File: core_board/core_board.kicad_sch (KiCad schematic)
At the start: 16 parts

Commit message: small updates
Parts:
- removed J?: Conn_01x04_Male, symbol Connector:Conn_01x04_Male
- removed J? (x6): Conn_02x25_Top_Bottom, symbol Connector_Generic:Conn_02x25_Top_Bottom
- added J?: Dsub, symbol Connector_Generic:Conn_02x25_Top_Bottom
- added R?: 10k, symbol Device:R_Small_US
- added U?: TCA9535PWR, SOP65P640X120-24N, symbol TCA9535PWR:TCA9535PWR
- J?: value Conn_01x03_Male -> UART Pins
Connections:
- net +3V3: now also R?.1, U?.24 (VCC)
- net GND: now also U?.12 (GND), U?.2 (A1), U?.21 (A0), U?.3 (A2)
- net Extra_Input_A renamed INT_0
- net INT_0: now also R?.2, U?.1 (~{INT})
- net Extra_Input_B renamed INT_1
- net Extra_Input_C renamed INT_2
- net Extra_Input_D renamed INT_3
- net I2C_SCL_A renamed I2C_SCL_0
- net I2C_SCL_B renamed I2C_SCL_1
- net I2C_SCL_C renamed I2C_SCL_2
- net I2C_SCL_Expander_A renamed Broadcast_A
- net I2C_SCL_Expander_B renamed Broadcast_C
- net I2C_SDA_A renamed I2C_SDA_1
- net I2C_SDA_B renamed I2C_SDA_2
- net I2C_SDA_C renamed I2C_SDA_3
- net I2C_SDA_Expander_A renamed INT_5
- net I2C_SDA_Expander_B renamed Broadcast_B
- net IGNITE renamed INT_4
- net SPI_CS_0 renamed I2C_SDA_0
- net SPI_CS_1 renamed I2C_SCL_3
- net SPI_CS_2 renamed I2C_SDA_4
- net SPI_CS_3 renamed I2C_SCL_4
- net SPI_CS_4 renamed I2C_SDA_5
- net SPI_CS_5 renamed I2C_SCL_5
- net SPI_MISO renamed I2C_SDA_IO_Expander
- net I2C_SDA_IO_Expander: now also U?.23 (SDA)
- net SPI_MOSI renamed I2C_SCL_IO_Expander
- net I2C_SCL_IO_Expander: now also U?.22 (SCL)
- net SPI_SCK renamed Broadcast_D
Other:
- note added: "TODO: Add pullip resistors for I2C and I/O"
- note added: "TODO: Add testpoints for logic analyzer"
- note removed: "TODO: Add I/O Expanders"
- note removed: "TODO: Add components for DC-DC converter"
- moved on the sheet: JP?, R?, U?

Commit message: finished schematic
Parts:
- removed D?: D_Schottky, symbol Device:D_Schottky
- removed R?: 10k, symbol Device:R_Small_US
- removed U?: TPS54332DDAR, VREG_LM5017MR/NOPB, symbol TPS54332DDAR:TPS54332DDAR
- added C? (x2): 10uF, symbol Device:C_Small
- added C? (x4): 47uF, symbol Device:C_Small
- added C?: 145pF, symbol Device:C_Small
- added C?: 90pF, symbol Device:C_Small
- added C?: 5pF, symbol Device:C_Small
- added C?: 8pF, symbol Device:C_Small
- added C? (x2): 15nF, symbol Device:C_Small
- added C? (x2): 0.1uF, symbol Device:C_Small
- added D? (x2): B340, Diode_SMD:D_SMC, symbol Diode:B340
- added D?: 40V, Diode_SMD:D_0603_1608Metric, symbol Device:D_Schottky
- added J? (x5): Dsub, symbol Connector_Generic:Conn_02x25_Top_Bottom
- added J?: Testpoints, symbol Connector_Generic:Conn_02x10_Odd_Even
- added L?: 2.85uH, symbol Device:L_Small
- added L?: 3.5uH, symbol Device:L_Small
- added R? (x14): 4.7k, symbol Device:R_Small_US
- added R? (x3): 150k, symbol Device:R_Small_US
- added R? (x8): 10k, symbol Device:R_Small_US
- added R? (x2): 1M, symbol Device:R_Small_US
- added R?: 3.2k, symbol Device:R_Small_US
- added R?: 95k, symbol Device:R_Small_US
- added R? (x2): 50k, symbol Device:R_Small_US
- added R?: 1.9k, symbol Device:R_Small_US
- added U? (x5): TCA9535PWR, SOP65P640X120-24N, symbol TCA9535PWR:TCA9535PWR
- added U?: TPS54332DDAR, VREG_LM5017MR/NOPB, symbol TPS54332DDAR:TPS54332DDAR
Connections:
- net +12V is gone; now on net 12V: J?.2 (Pin_2), U?.2 (VIN)
- net +3V3 is gone; now on net 3V3: U?.24 (VCC)
- net Broadcast_A: now also J?.3 (Pin_3), U?.15 (IO13), J?.15 (Pin_15), J?.3 (Pin_3), J?.3 (Pin_3), J?.3 (Pin_3), J?.3 (Pin_3), J?.3 (Pin_3); no longer U?.9 (IO25)
- net Broadcast_B: now also J?.4 (Pin_4), U?.13 (IO12), J?.16 (Pin_16), J?.4 (Pin_4), J?.4 (Pin_4), J?.4 (Pin_4), J?.4 (Pin_4), J?.4 (Pin_4); no longer U?.10 (IO26)
- net Broadcast_C: now also J?.5 (Pin_5), U?.10 (IO26), J?.17 (Pin_17), J?.5 (Pin_5), J?.5 (Pin_5), J?.5 (Pin_5), J?.5 (Pin_5), J?.5 (Pin_5); no longer U?.11 (IO27)
- net Broadcast_D: now also J?.6 (Pin_6), U?.9 (IO25), J?.18 (Pin_18), J?.6 (Pin_6), J?.6 (Pin_6), J?.6 (Pin_6), J?.6 (Pin_6), J?.6 (Pin_6); no longer U?.12 (IO14)
- net GND: now also J?.1 (Pin_1), J?.23 (Pin_23), J?.24 (Pin_24), J?.25 (Pin_25), J?.26 (Pin_26), J?.27 (Pin_27), J?.28 (Pin_28), J?.29 (Pin_29), C?.1, C?.1, C?.1, C?.1, C?.2, C?.2, C?.2, C?.2, C?.2, C?.2, D?.2 (A), D?.2 (A), D?.2 (A), J?.19 (Pin_19), J?.20 (Pin_20), J?.23 (Pin_23), J?.23 (Pin_23), J?.23 (Pin_23), J?.23 (Pin_23), J?.23 (Pin_23), J?.24 (Pin_24), J?.24 (Pin_24), J?.24 (Pin_24), J?.24 (Pin_24), J?.24 (Pin_24), J?.25 (Pin_25), J?.25 (Pin_25), J?.25 (Pin_25), J?.25 (Pin_25), J?.25 (Pin_25), J?.26 (Pin_26), J?.26 (Pin_26), J?.26 (Pin_26), J?.26 (Pin_26), J?.26 (Pin_26), J?.27 (Pin_27), J?.27 (Pin_27), J?.27 (Pin_27), J?.27 (Pin_27), J?.27 (Pin_27), J?.28 (Pin_28), J?.28 (Pin_28), J?.28 (Pin_28), J?.28 (Pin_28), J?.28 (Pin_28), J?.29 (Pin_29), J?.29 (Pin_29), J?.29 (Pin_29), J?.29 (Pin_29), J?.29 (Pin_29), R?.1, R?.1, R?.1, R?.1, R?.1, R?.1, R?.2, R?.2, U?.12 (GND), U?.12 (GND), U?.12 (GND), U?.12 (GND), U?.12 (GND), U?.2 (A1), U?.2 (A1), U?.2 (A1), U?.2 (A1), U?.21 (A0), U?.21 (A0), U?.21 (A0), U?.3 (A2), U?.3 (A2), U?.3 (A2), U?.7 (GND), U?.9 (EP); no longer U?.2 (A1), U?.21 (A0)
- net I2C_SCL_0: now also U?.21 (IO23), J?.2 (Pin_2), J?.2 (Pin_2), R?.2; no longer U?.22 (IO22)
- net I2C_SCL_1: now also U?.22 (IO22), J?.2 (Pin_2), J?.4 (Pin_4), R?.2; no longer U?.27 (IO19)
- net I2C_SCL_2: now also U?.28 (IO18), J?.2 (Pin_2), J?.6 (Pin_6), R?.2; no longer U?.29 (IO5)
- net I2C_SCL_3: now also J?.2 (Pin_2), U?.30 (IO17), J?.8 (Pin_8), R?.2; no longer U?.31 (IO16)
- net I2C_SCL_4: now also U?.32 (IO4), J?.10 (Pin_10), J?.2 (Pin_2), R?.2; no longer U?.33 (IO0)
- net I2C_SCL_5: now also U?.34 (IO2), J?.12 (Pin_12), J?.2 (Pin_2), R?.2; no longer U?.35 (IO15)
- net I2C_SDA_0: now also U?.25 (IO21), J?.1 (Pin_1), J?.1 (Pin_1), R?.2; no longer U?.21 (IO23)
- net I2C_SDA_1: now also U?.27 (IO19), J?.1 (Pin_1), J?.3 (Pin_3), R?.2; no longer U?.25 (IO21)
- net I2C_SDA_2: now also U?.29 (IO5), J?.1 (Pin_1), J?.5 (Pin_5), R?.2; no longer U?.28 (IO18)
- net I2C_SDA_3: now also J?.1 (Pin_1), U?.31 (IO16), J?.7 (Pin_7), R?.2; no longer U?.30 (IO17)
- net I2C_SDA_4: now also U?.33 (IO0), J?.1 (Pin_1), J?.9 (Pin_9), R?.2; no longer U?.32 (IO4)
- net I2C_SDA_5: now also U?.35 (IO15), J?.1 (Pin_1), J?.11 (Pin_11), R?.2; no longer U?.34 (IO2)
- net INT_0: now also R?.2, U?.1 (~{INT}); no longer U?.1 (~{INT})
- net INT_1: now also R?.2, U?.1 (~{INT})
- net INT_2: now also R?.2, U?.1 (~{INT})
- net INT_3: now also U?.1 (~{INT}), R?.2
- net INT_4: now also R?.2, U?.1 (~{INT})
- net INT_5: now also R?.2, U?.1 (~{INT})
- net IO_3_06: now reaches U?.10 (P06)
- net IO_3_06: now also J?.13 (Pin_13)
- net IO_3_07: now reaches U?.11 (P07)
- net IO_3_07: now also J?.14 (Pin_14)
- net IO_3_08: now reaches U?.13 (P10)
- net IO_3_08: now also J?.15 (Pin_15)
- net IO_3_09: now reaches U?.14 (P11)
- net IO_3_09: now also J?.16 (Pin_16)
- net IO_3_10: now reaches U?.15 (P12)
- net IO_3_10: now also J?.17 (Pin_17)
- net IO_3_11: now reaches U?.16 (P13)
- net IO_3_11: now also J?.18 (Pin_18)
- net IO_3_12: now reaches U?.17 (P14)
- net IO_3_12: now also J?.19 (Pin_19)
- net IO_3_13: now reaches U?.18 (P15)
- net IO_3_13: now also J?.20 (Pin_20)
- net IO_3_14: now reaches U?.19 (P16)
- net IO_3_14: now also J?.21 (Pin_21)
- net IO_3_15: now reaches U?.20 (P17)
- net IO_3_15: now also J?.22 (Pin_22)
- net IO_3_00: now reaches U?.4 (P00)
- net IO_3_00: now also J?.7 (Pin_7)
- net IO_3_01: now reaches U?.5 (P01)
- net IO_3_01: now also J?.8 (Pin_8)
- net IO_3_02: now reaches U?.6 (P02)
- net IO_3_02: now also J?.9 (Pin_9)
- net IO_3_03: now reaches U?.7 (P03)
- net IO_3_03: now also J?.10 (Pin_10)
- net IO_3_04: now reaches U?.8 (P04)
- net IO_3_04: now also J?.11 (Pin_11)
- net IO_3_05: now reaches U?.9 (P05)
- net IO_3_05: now also J?.12 (Pin_12)
- net at U?.1 (BOOT): now also C?.2
- net at U?.3 (EN): now also R?.1, R?.2
- net at U?.4 (SS): now also C?.2, R?.2
- net at U?.5 (VSENSE): now also R?.1, R?.2
- net at U?.6 (COMP): now also C?.2, C?.2
- net at U?.8 (PH): now also C?.1, D?.1 (K), L?.1
- net 3V3: now reaches J?.30 (Pin_30)
- net 3V3: now also J?.31 (Pin_31), J?.32 (Pin_32), J?.33 (Pin_33), J?.34 (Pin_34), J?.35 (Pin_35), J?.36 (Pin_36), U?.2 (A1), U?.21 (A0), C?.1, C?.1, J?.30 (Pin_30), J?.30 (Pin_30), J?.30 (Pin_30), J?.30 (Pin_30), J?.30 (Pin_30), J?.31 (Pin_31), J?.31 (Pin_31), J?.31 (Pin_31), J?.31 (Pin_31), J?.31 (Pin_31), J?.32 (Pin_32), J?.32 (Pin_32), J?.32 (Pin_32), J?.32 (Pin_32), J?.32 (Pin_32), J?.33 (Pin_33), J?.33 (Pin_33), J?.33 (Pin_33), J?.33 (Pin_33), J?.33 (Pin_33), J?.34 (Pin_34), J?.34 (Pin_34), J?.34 (Pin_34), J?.34 (Pin_34), J?.34 (Pin_34), J?.35 (Pin_35), J?.35 (Pin_35), J?.35 (Pin_35), J?.35 (Pin_35), J?.35 (Pin_35), J?.36 (Pin_36), J?.36 (Pin_36), J?.36 (Pin_36), J?.36 (Pin_36), J?.36 (Pin_36), L?.2, R?.1, R?.1, R?.1, R?.1, R?.1, R?.1, R?.1, R?.1, R?.1, R?.1, R?.1, R?.1, R?.1, R?.1, R?.1, R?.1, R?.1, R?.1, R?.1, R?.1, R?.2, U?.2 (A1), U?.21 (A0), U?.21 (A0), U?.24 (VCC), U?.24 (VCC), U?.24 (VCC), U?.24 (VCC), U?.24 (VCC), U?.3 (A2), U?.3 (A2)
- net 5V: now reaches J?.37 (Pin_37)
- net 5V: now also J?.38 (Pin_38), J?.39 (Pin_39), J?.40 (Pin_40), J?.41 (Pin_41), J?.42 (Pin_42), J?.43 (Pin_43), JP?.1 (A), C?.1, C?.1, J?.37 (Pin_37), J?.37 (Pin_37), J?.37 (Pin_37), J?.37 (Pin_37), J?.37 (Pin_37), J?.38 (Pin_38), J?.38 (Pin_38), J?.38 (Pin_38), J?.38 (Pin_38), J?.38 (Pin_38), J?.39 (Pin_39), J?.39 (Pin_39), J?.39 (Pin_39), J?.39 (Pin_39), J?.39 (Pin_39), J?.40 (Pin_40), J?.40 (Pin_40), J?.40 (Pin_40), J?.40 (Pin_40), J?.40 (Pin_40), J?.41 (Pin_41), J?.41 (Pin_41), J?.41 (Pin_41), J?.41 (Pin_41), J?.41 (Pin_41), J?.42 (Pin_42), J?.42 (Pin_42), J?.42 (Pin_42), J?.42 (Pin_42), J?.42 (Pin_42), J?.43 (Pin_43), J?.43 (Pin_43), J?.43 (Pin_43), J?.43 (Pin_43), J?.43 (Pin_43), L?.2, R?.2
- net 12V: now reaches J?.44 (Pin_44)
- net 12V: now also J?.45 (Pin_45), J?.46 (Pin_46), J?.47 (Pin_47), J?.48 (Pin_48), J?.49 (Pin_49), J?.50 (Pin_50), C?.1, C?.1, D?.1 (K), J?.44 (Pin_44), J?.44 (Pin_44), J?.44 (Pin_44), J?.44 (Pin_44), J?.44 (Pin_44), J?.45 (Pin_45), J?.45 (Pin_45), J?.45 (Pin_45), J?.45 (Pin_45), J?.45 (Pin_45), J?.46 (Pin_46), J?.46 (Pin_46), J?.46 (Pin_46), J?.46 (Pin_46), J?.46 (Pin_46), J?.47 (Pin_47), J?.47 (Pin_47), J?.47 (Pin_47), J?.47 (Pin_47), J?.47 (Pin_47), J?.48 (Pin_48), J?.48 (Pin_48), J?.48 (Pin_48), J?.48 (Pin_48), J?.48 (Pin_48), J?.49 (Pin_49), J?.49 (Pin_49), J?.49 (Pin_49), J?.49 (Pin_49), J?.49 (Pin_49), J?.50 (Pin_50), J?.50 (Pin_50), J?.50 (Pin_50), J?.50 (Pin_50), J?.50 (Pin_50), R?.2, R?.2, U?.2 (VIN)
- removed net +5V: J?.1 (Pin_1), JP?.1 (A)
- net I2C_SCL_IO_Expander renamed I2C_SCL_Exp
- net I2C_SCL_Exp: now also U?.11 (IO27), J?.14 (Pin_14), R?.2, U?.22 (SCL), U?.22 (SCL), U?.22 (SCL), U?.22 (SCL), U?.22 (SCL); no longer U?.15 (IO13)
- net I2C_SDA_IO_Expander renamed I2C_SDA_Exp
- net I2C_SDA_Exp: now also U?.12 (IO14), J?.13 (Pin_13), R?.2, U?.23 (SDA), U?.23 (SDA), U?.23 (SDA), U?.23 (SDA), U?.23 (SDA); no longer U?.13 (IO12)
- new net: C?.1, D?.1 (K), L?.1, U?.8 (PH)
- new net: R?.1, R?.2, U?.3 (EN)
- new net: R?.1, R?.2, U?.5 (VSENSE)
- new net: C?.1, R?.1 (x2)
- new net: C?.2, R?.2, U?.4 (SS)
- new net: C?.2, C?.2, U?.6 (COMP)
- new net: C?.2, U?.1 (BOOT)
- new net IO_0_00: J?.7 (Pin_7), U?.4 (P00)
- new net IO_0_01: J?.8 (Pin_8), U?.5 (P01)
- new net IO_0_02: J?.9 (Pin_9), U?.6 (P02)
- new net IO_0_03: J?.10 (Pin_10), U?.7 (P03)
- new net IO_0_04: J?.11 (Pin_11), U?.8 (P04)
- new net IO_0_05: J?.12 (Pin_12), U?.9 (P05)
- new net IO_0_06: J?.13 (Pin_13), U?.10 (P06)
- new net IO_0_07: J?.14 (Pin_14), U?.11 (P07)
- new net IO_0_08: J?.15 (Pin_15), U?.13 (P10)
- new net IO_0_09: J?.16 (Pin_16), U?.14 (P11)
- new net IO_0_10: J?.17 (Pin_17), U?.15 (P12)
- new net IO_0_11: J?.18 (Pin_18), U?.16 (P13)
- new net IO_0_12: J?.19 (Pin_19), U?.17 (P14)
- new net IO_0_13: J?.20 (Pin_20), U?.18 (P15)
- new net IO_0_14: J?.21 (Pin_21), U?.19 (P16)
- new net IO_0_15: J?.22 (Pin_22), U?.20 (P17)
- new net IO_1_00: J?.7 (Pin_7), U?.4 (P00)
- new net IO_1_01: J?.8 (Pin_8), U?.5 (P01)
- new net IO_1_02: J?.9 (Pin_9), U?.6 (P02)
- new net IO_1_03: J?.10 (Pin_10), U?.7 (P03)
- new net IO_1_04: J?.11 (Pin_11), U?.8 (P04)
- new net IO_1_05: J?.12 (Pin_12), U?.9 (P05)
- new net IO_1_06: J?.13 (Pin_13), U?.10 (P06)
- new net IO_1_07: J?.14 (Pin_14), U?.11 (P07)
- new net IO_1_08: J?.15 (Pin_15), U?.13 (P10)
- new net IO_1_09: J?.16 (Pin_16), U?.14 (P11)
- new net IO_1_10: J?.17 (Pin_17), U?.15 (P12)
- new net IO_1_11: J?.18 (Pin_18), U?.16 (P13)
- new net IO_1_12: J?.19 (Pin_19), U?.17 (P14)
- new net IO_1_13: J?.20 (Pin_20), U?.18 (P15)
- new net IO_1_14: J?.21 (Pin_21), U?.19 (P16)
- new net IO_1_15: J?.22 (Pin_22), U?.20 (P17)
- new net IO_2_00: J?.7 (Pin_7), U?.4 (P00)
- new net IO_2_01: J?.8 (Pin_8), U?.5 (P01)
- new net IO_2_02: J?.9 (Pin_9), U?.6 (P02)
- new net IO_2_03: J?.10 (Pin_10), U?.7 (P03)
- new net IO_2_04: J?.11 (Pin_11), U?.8 (P04)
- new net IO_2_05: J?.12 (Pin_12), U?.9 (P05)
- new net IO_2_06: J?.13 (Pin_13), U?.10 (P06)
- new net IO_2_07: J?.14 (Pin_14), U?.11 (P07)
- new net IO_2_08: J?.15 (Pin_15), U?.13 (P10)
- new net IO_2_09: J?.16 (Pin_16), U?.14 (P11)
- new net IO_2_10: J?.17 (Pin_17), U?.15 (P12)
- new net IO_2_11: J?.18 (Pin_18), U?.16 (P13)
- new net IO_2_12: J?.19 (Pin_19), U?.17 (P14)
- new net IO_2_13: J?.20 (Pin_20), U?.18 (P15)
- new net IO_2_14: J?.21 (Pin_21), U?.19 (P16)
- new net IO_2_15: J?.22 (Pin_22), U?.20 (P17)
- new net IO_4_00: J?.7 (Pin_7), U?.4 (P00)
- new net IO_4_01: J?.8 (Pin_8), U?.5 (P01)
- new net IO_4_02: J?.9 (Pin_9), U?.6 (P02)
- new net IO_4_03: J?.10 (Pin_10), U?.7 (P03)
- new net IO_4_04: J?.11 (Pin_11), U?.8 (P04)
- new net IO_4_05: J?.12 (Pin_12), U?.9 (P05)
- new net IO_4_06: J?.13 (Pin_13), U?.10 (P06)
- new net IO_4_07: J?.14 (Pin_14), U?.11 (P07)
- new net IO_4_08: J?.15 (Pin_15), U?.13 (P10)
- new net IO_4_09: J?.16 (Pin_16), U?.14 (P11)
- new net IO_4_10: J?.17 (Pin_17), U?.15 (P12)
- new net IO_4_11: J?.18 (Pin_18), U?.16 (P13)
- new net IO_4_12: J?.19 (Pin_19), U?.17 (P14)
- new net IO_4_13: J?.20 (Pin_20), U?.18 (P15)
- new net IO_4_14: J?.21 (Pin_21), U?.19 (P16)
- new net IO_4_15: J?.22 (Pin_22), U?.20 (P17)
- new net IO_5_00: J?.7 (Pin_7), U?.4 (P00)
- new net IO_5_01: J?.8 (Pin_8), U?.5 (P01)
- new net IO_5_02: J?.9 (Pin_9), U?.6 (P02)
- new net IO_5_03: J?.10 (Pin_10), U?.7 (P03)
- new net IO_5_04: J?.11 (Pin_11), U?.8 (P04)
- new net IO_5_05: J?.12 (Pin_12), U?.9 (P05)
- new net IO_5_06: J?.13 (Pin_13), U?.10 (P06)
- new net IO_5_07: J?.14 (Pin_14), U?.11 (P07)
- new net IO_5_08: J?.15 (Pin_15), U?.13 (P10)
- new net IO_5_09: J?.16 (Pin_16), U?.14 (P11)
- new net IO_5_10: J?.17 (Pin_17), U?.15 (P12)
- new net IO_5_11: J?.18 (Pin_18), U?.16 (P13)
- new net IO_5_12: J?.19 (Pin_19), U?.17 (P14)
- new net IO_5_13: J?.20 (Pin_20), U?.18 (P15)
- new net IO_5_14: J?.21 (Pin_21), U?.19 (P16)
- new net IO_5_15: J?.22 (Pin_22), U?.20 (P17)
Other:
- note added: "Do I/O pins need pullup resistors?"
- note added: "Should we add overvoltage protection fuse?"
- note removed: "TODO: Add pullip resistors for I2C and I/O"
- note removed: "TODO: Add testpoints for logic analyzer"
- moved on the sheet: J?, JP?, R?, U?

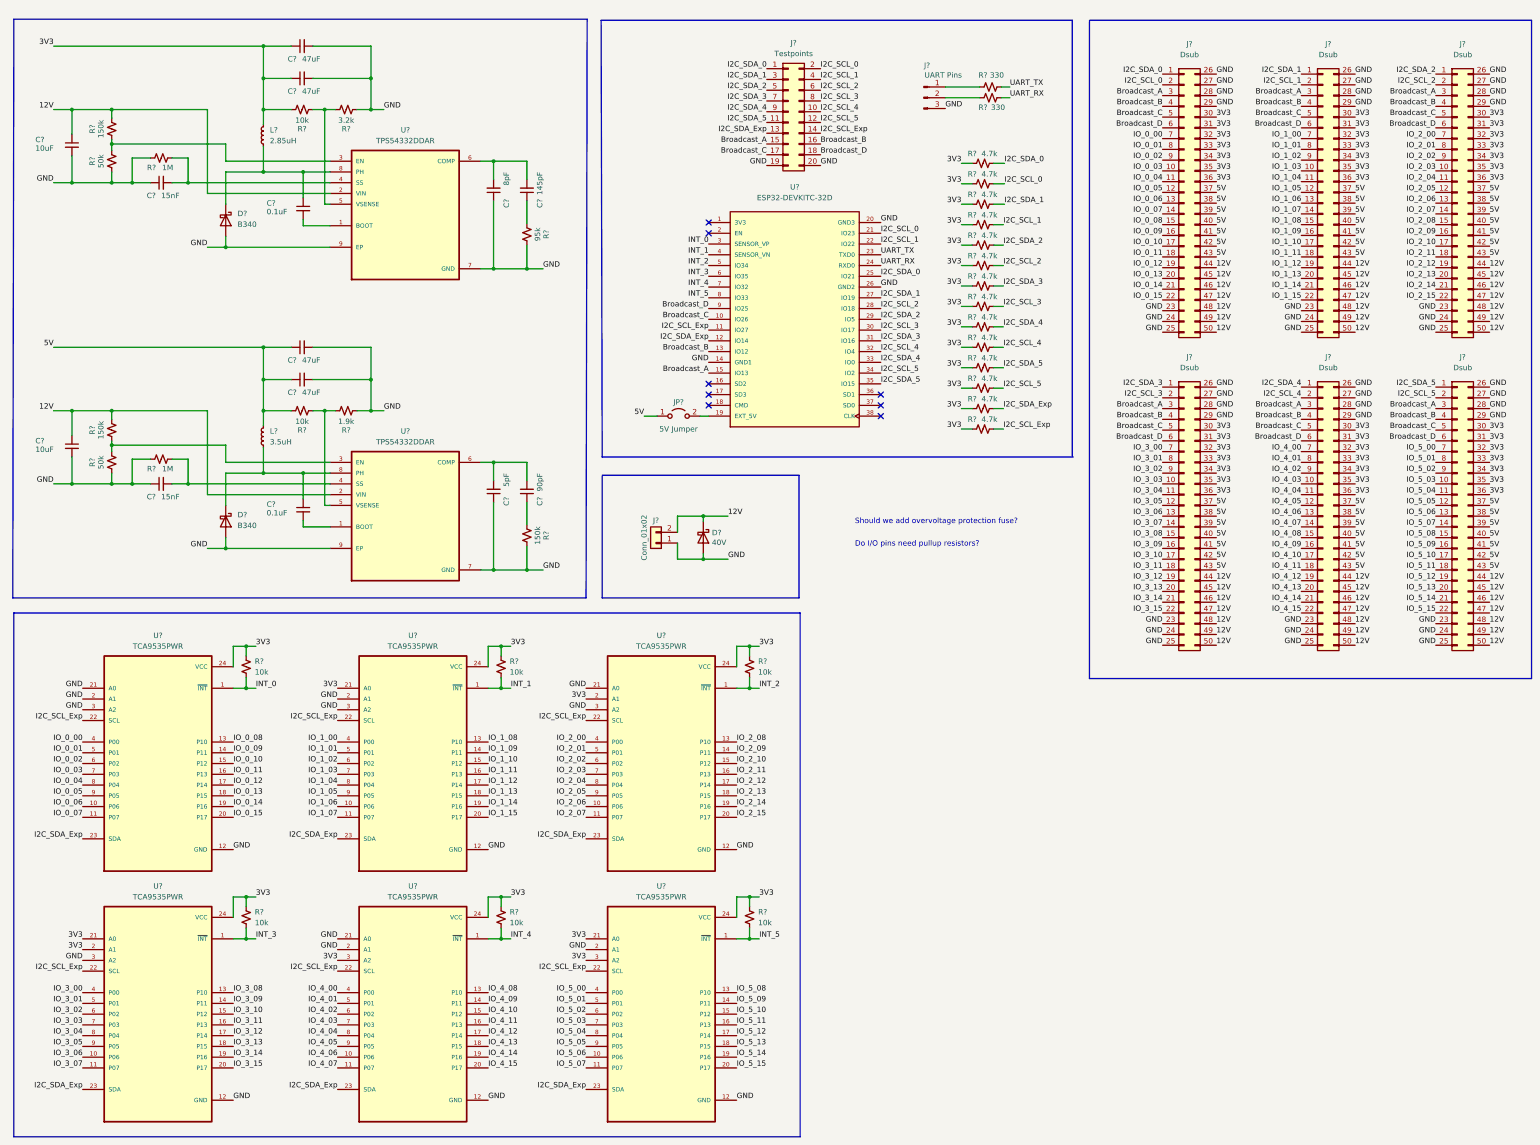
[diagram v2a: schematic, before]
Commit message: updated to 15-pin dsub
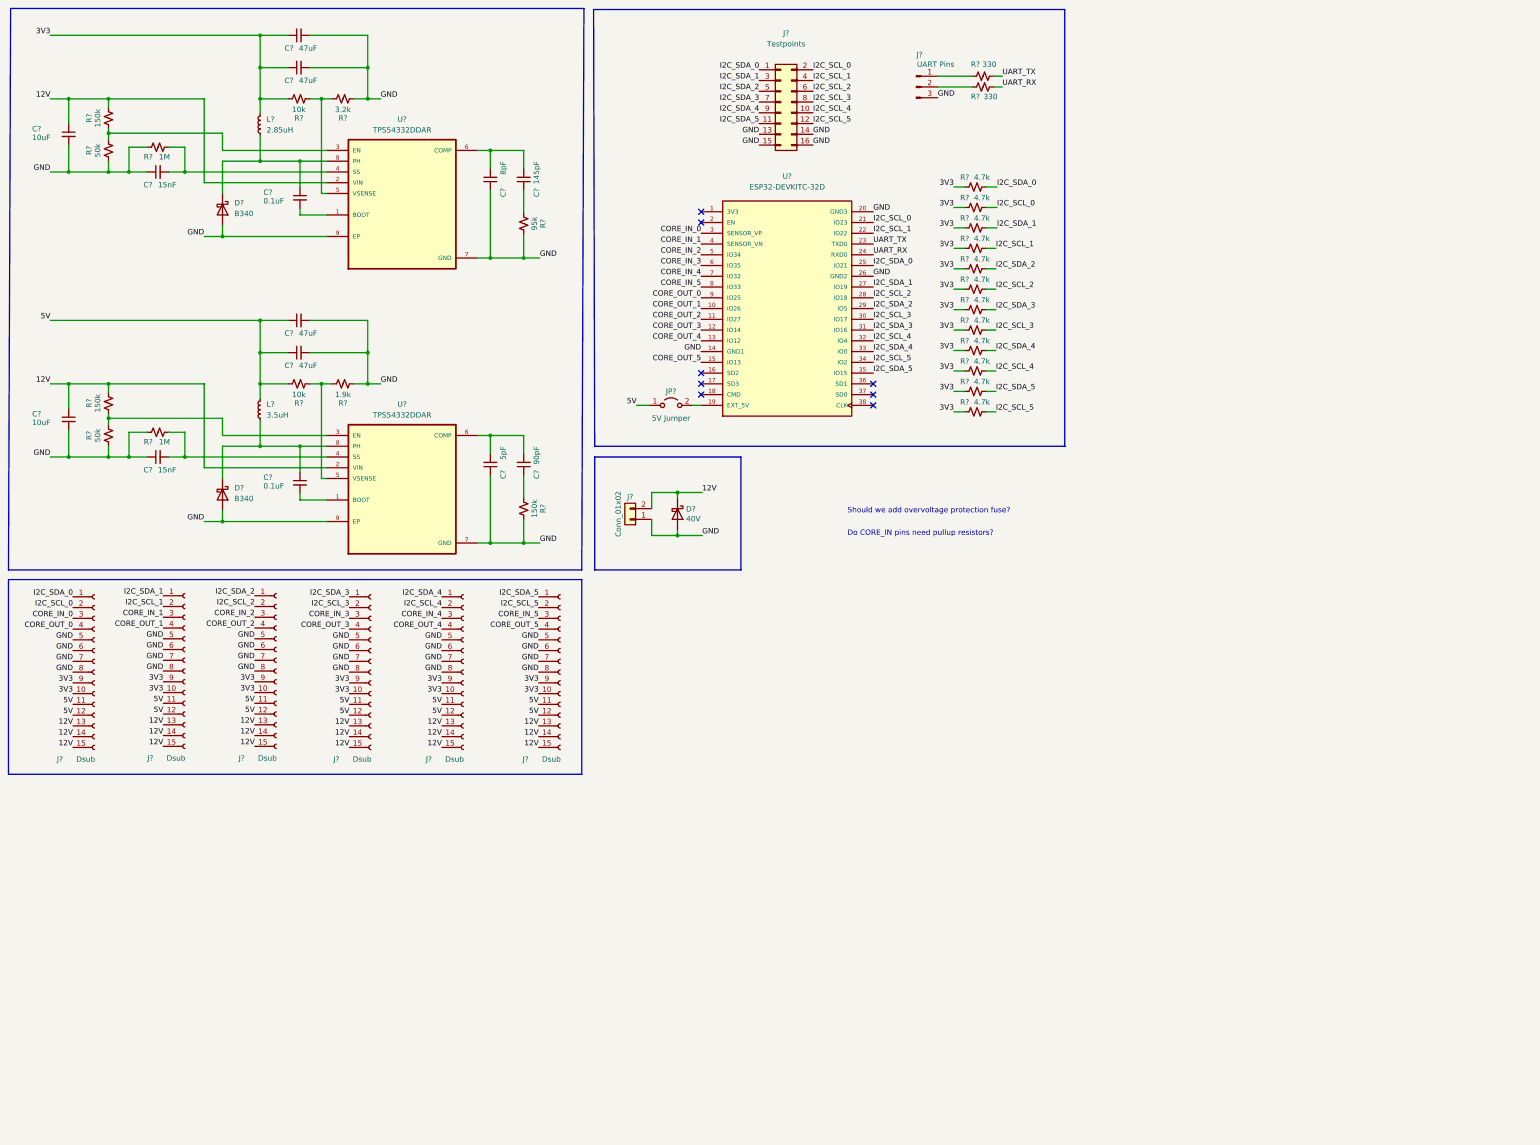
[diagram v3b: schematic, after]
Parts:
- removed J? (x6): Dsub, symbol Connector_Generic:Conn_02x25_Top_Bottom
- removed R? (x2): 4.7k, symbol Device:R_Small_US
- removed R? (x6): 10k, symbol Device:R_Small_US
- removed U? (x6): TCA9535PWR, SOP65P640X120-24N, symbol TCA9535PWR:TCA9535PWR
- added J? (x6): Dsub, symbol Connector:Conn_01x15_Female
- J?: symbol Connector_Generic:Conn_02x10_Odd_Even -> Connector_Generic:Conn_02x08_Odd_Even
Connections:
- net 12V: now also J?.13 (Pin_13), J?.13 (Pin_13), J?.13 (Pin_13), J?.13 (Pin_13), J?.13 (Pin_13), J?.13 (Pin_13), J?.14 (Pin_14), J?.14 (Pin_14), J?.14 (Pin_14), J?.14 (Pin_14), J?.14 (Pin_14), J?.14 (Pin_14), J?.15 (Pin_15), J?.15 (Pin_15), J?.15 (Pin_15), J?.15 (Pin_15), J?.15 (Pin_15), J?.15 (Pin_15)
- net 3V3: now also J?.10 (Pin_10), J?.10 (Pin_10), J?.10 (Pin_10), J?.10 (Pin_10), J?.10 (Pin_10), J?.10 (Pin_10), J?.9 (Pin_9), J?.9 (Pin_9), J?.9 (Pin_9), J?.9 (Pin_9), J?.9 (Pin_9), J?.9 (Pin_9)
- net 5V: now also J?.11 (Pin_11), J?.11 (Pin_11), J?.11 (Pin_11), J?.11 (Pin_11), J?.11 (Pin_11), J?.11 (Pin_11), J?.12 (Pin_12), J?.12 (Pin_12), J?.12 (Pin_12), J?.12 (Pin_12), J?.12 (Pin_12), J?.12 (Pin_12)
- net GND: now also J?.13 (Pin_13), J?.14 (Pin_14), J?.15 (Pin_15), J?.16 (Pin_16), J?.5 (Pin_5), J?.5 (Pin_5), J?.5 (Pin_5), J?.5 (Pin_5), J?.5 (Pin_5), J?.5 (Pin_5), J?.6 (Pin_6), J?.6 (Pin_6), J?.6 (Pin_6), J?.6 (Pin_6), J?.6 (Pin_6), J?.6 (Pin_6), J?.7 (Pin_7), J?.7 (Pin_7), J?.7 (Pin_7), J?.7 (Pin_7), J?.7 (Pin_7), J?.7 (Pin_7), J?.8 (Pin_8), J?.8 (Pin_8), J?.8 (Pin_8), J?.8 (Pin_8), J?.8 (Pin_8), J?.8 (Pin_8); no longer J?.19 (Pin_19), J?.20 (Pin_20)
- net I2C_SCL_0: now also J?.2 (Pin_2)
- net I2C_SCL_1: now also J?.2 (Pin_2)
- net I2C_SCL_2: now also J?.2 (Pin_2)
- net I2C_SCL_3: now also J?.2 (Pin_2)
- net I2C_SCL_4: now also J?.2 (Pin_2)
- net I2C_SCL_5: now also J?.2 (Pin_2)
- net I2C_SDA_0: now also J?.1 (Pin_1)
- net I2C_SDA_1: now also J?.1 (Pin_1)
- net I2C_SDA_2: now also J?.1 (Pin_1)
- net I2C_SDA_3: now also J?.1 (Pin_1)
- net I2C_SDA_4: now also J?.1 (Pin_1)
- net I2C_SDA_5: now also J?.1 (Pin_1)
- net Broadcast_A renamed CORE_OUT_5
- net CORE_OUT_5: now also J?.4 (Pin_4); no longer J?.15 (Pin_15)
- net Broadcast_B renamed CORE_OUT_4
- net CORE_OUT_4: now also J?.4 (Pin_4); no longer J?.16 (Pin_16)
- net Broadcast_C renamed CORE_OUT_1
- net CORE_OUT_1: now also J?.4 (Pin_4); no longer J?.17 (Pin_17)
- net Broadcast_D renamed CORE_OUT_0
- net CORE_OUT_0: now also J?.4 (Pin_4); no longer J?.18 (Pin_18)
- net I2C_SCL_Exp renamed CORE_OUT_2
- net CORE_OUT_2: now also J?.4 (Pin_4); no longer J?.14 (Pin_14)
- net I2C_SDA_Exp renamed CORE_OUT_3
- net CORE_OUT_3: now also J?.4 (Pin_4); no longer J?.13 (Pin_13)
- net INT_0 renamed CORE_IN_0
- net CORE_IN_0: now also J?.3 (Pin_3)
- net INT_1 renamed CORE_IN_1
- net CORE_IN_1: now also J?.3 (Pin_3)
- net INT_2 renamed CORE_IN_2
- net CORE_IN_2: now also J?.3 (Pin_3)
- net INT_3 renamed CORE_IN_3
- net CORE_IN_3: now also J?.3 (Pin_3)
- net INT_4 renamed CORE_IN_4
- net CORE_IN_4: now also J?.3 (Pin_3)
- net INT_5 renamed CORE_IN_5
- net CORE_IN_5: now also J?.3 (Pin_3)
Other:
- note added: "Do CORE_IN pins need pullup resistors?"
- note removed: "Do I/O pins need pullup resistors?"
- moved on the sheet: C?, D?, J?, JP?, L?, R?, U?
